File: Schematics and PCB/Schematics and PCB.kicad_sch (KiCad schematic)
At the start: 0 parts

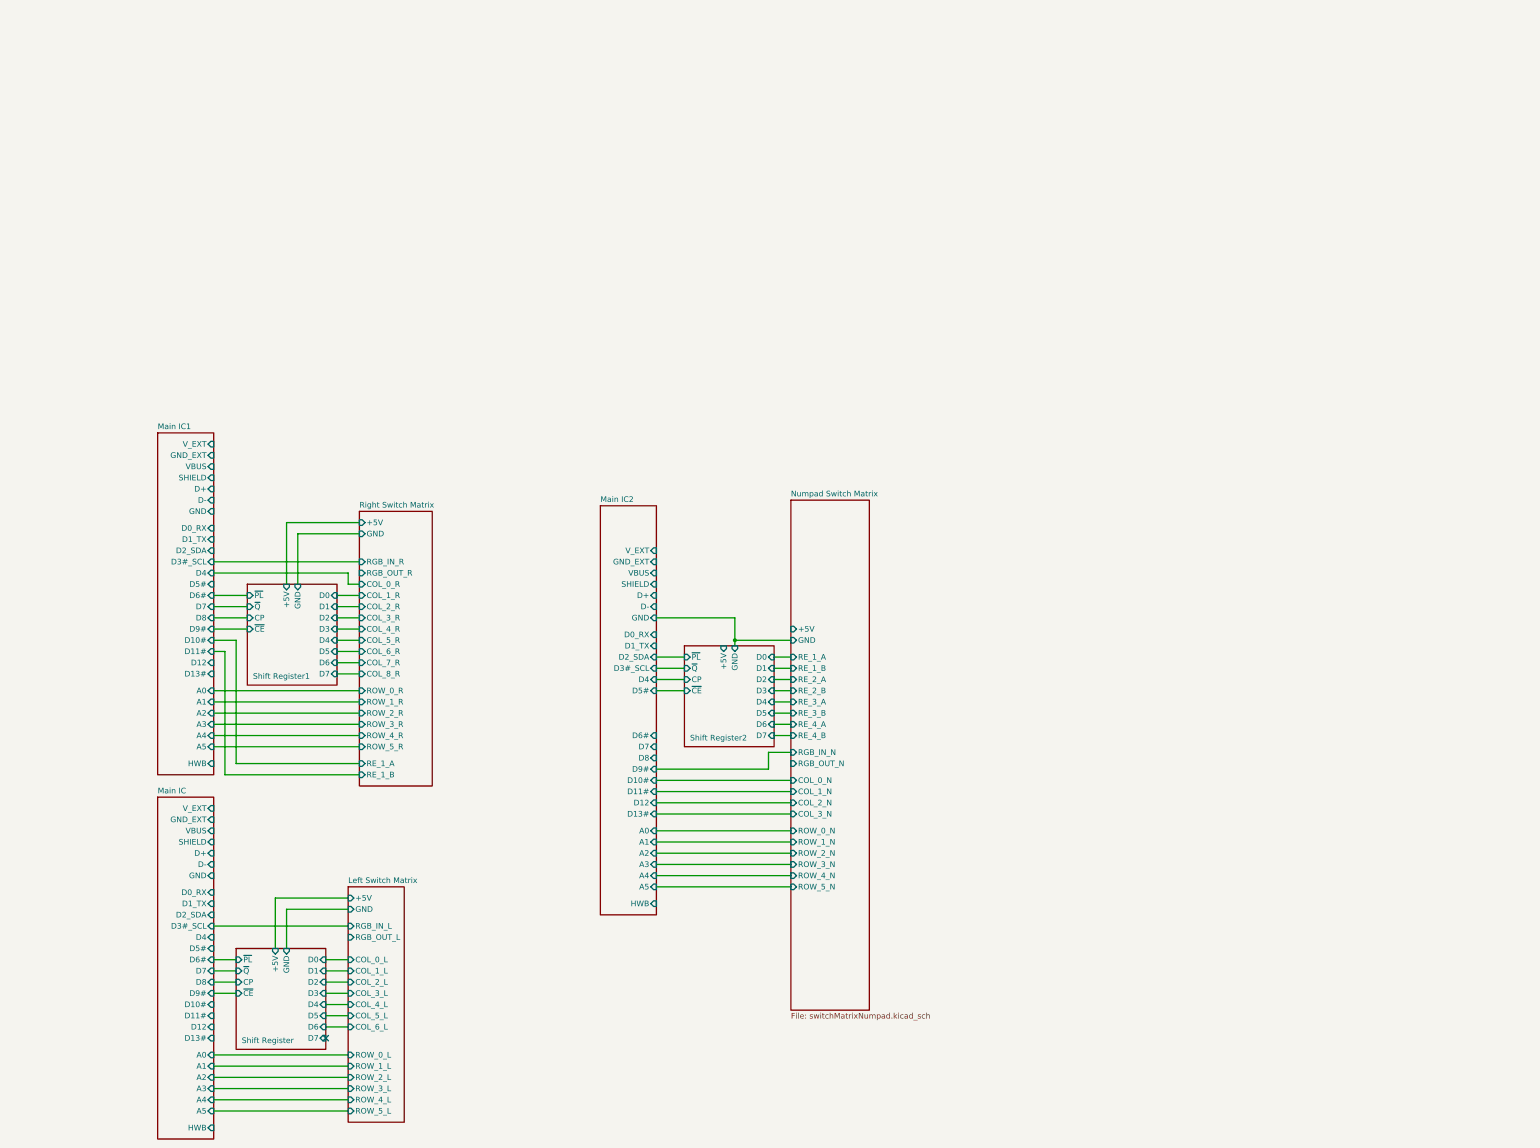
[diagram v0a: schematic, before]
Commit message: schematic progress
added li-po charge circuits and usb hub
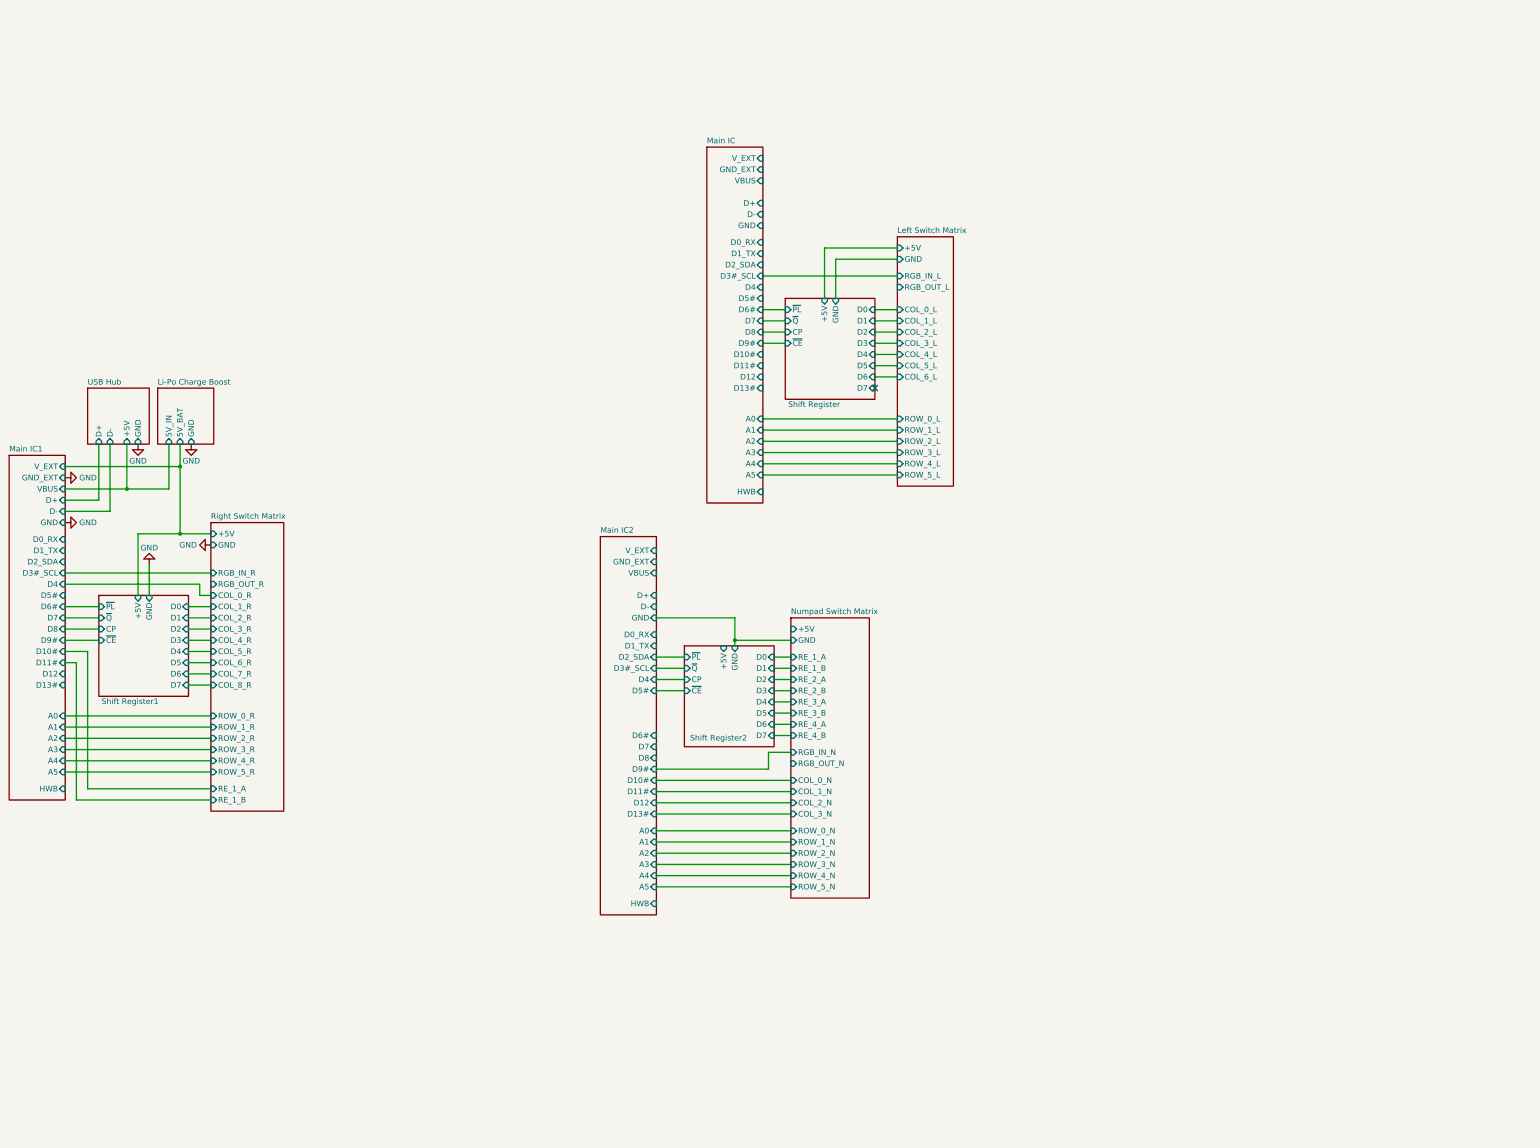
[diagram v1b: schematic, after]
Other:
- added sheet Li-Po Charge Boost (Li-Po_Charge_Boost.kicad_sch)
- added sheet USB Hub (USB_Hub.kicad_sch)
- sheet Main IC ports: added none; removed SHIELD
- sheet Main IC1 ports: added none; removed SHIELD
- sheet Main IC2 ports: added none; removed SHIELD

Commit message: compatibility commit
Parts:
- added J6: Magnetic Right, symbol Connector_Generic:Conn_01x05
- added J9: Magnetic Left, symbol Connector_Generic:Conn_01x05

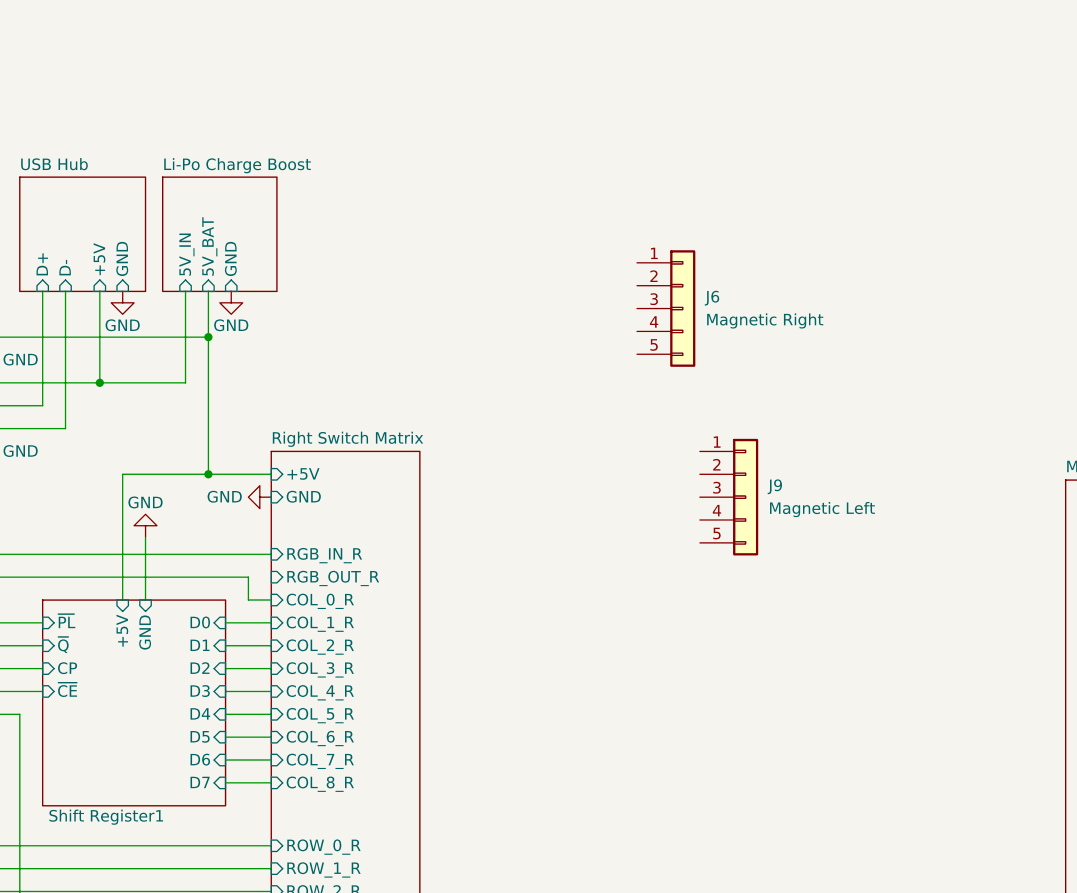
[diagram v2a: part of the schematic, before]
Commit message: Updated USB hub
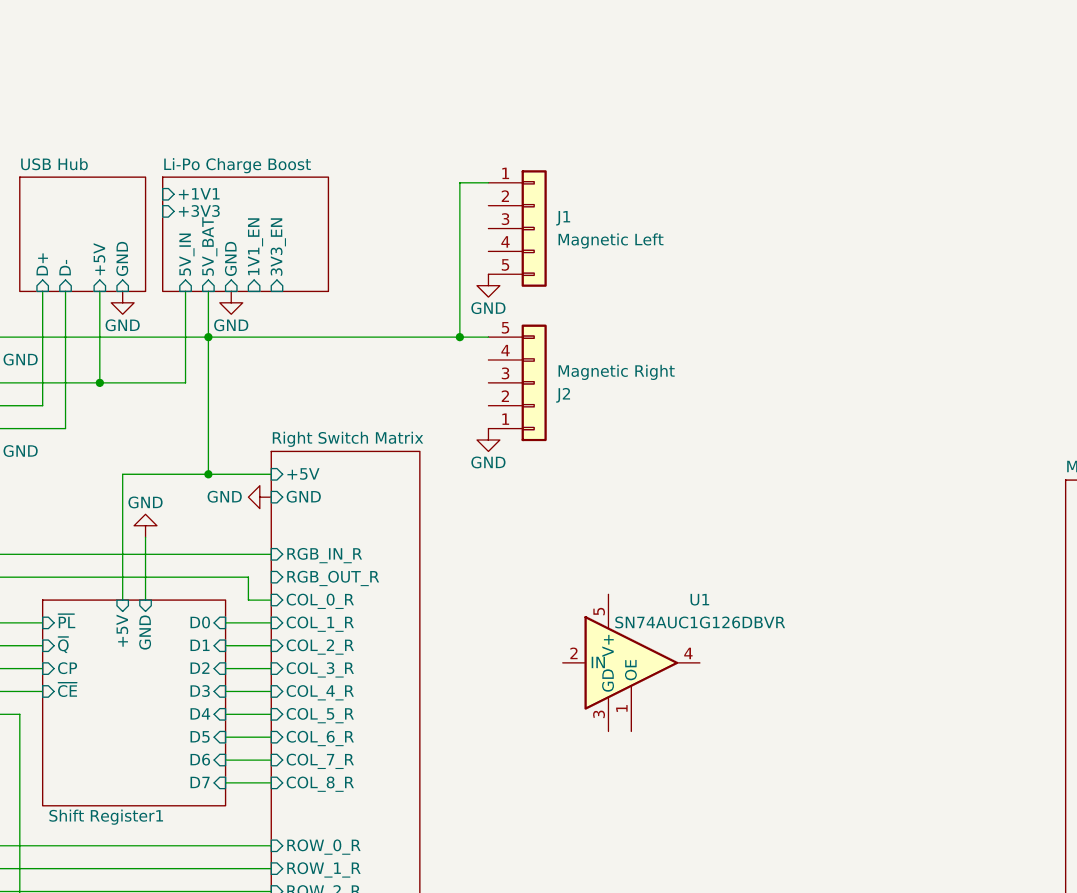
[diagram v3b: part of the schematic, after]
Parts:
- added U1: SN74AUC1G126DBVR, symbol mechpadLibrary:Tri-state_Buffer
- renumbered J9 to J1, J6 to J2
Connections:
- net GND: now also J1.5 (Pin_5), J2.1 (Pin_1)
- net Li-Po Charge Boost/5V_BAT: now also J1.1 (Pin_1), J2.5 (Pin_5)
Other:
- sheet Li-Po Charge Boost ports: added +1V1, +3V3, 1V1_EN, 3V3_EN; removed none
- moved on the sheet: J1, J2

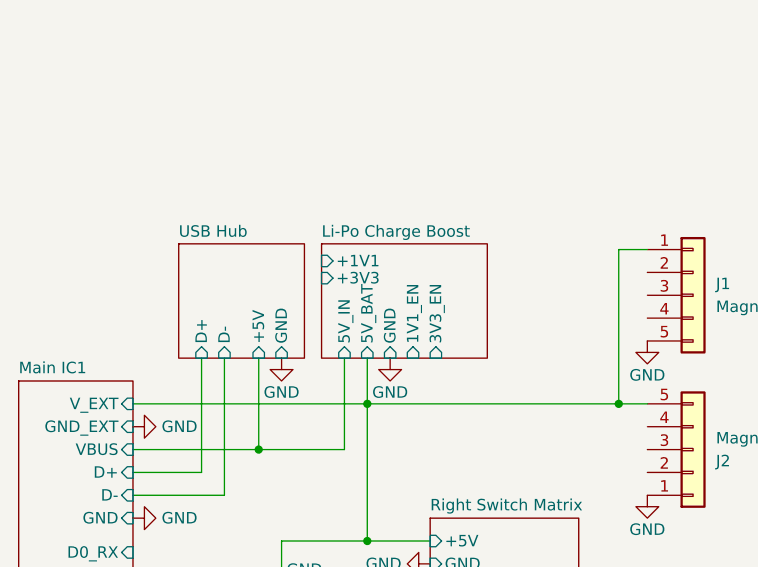
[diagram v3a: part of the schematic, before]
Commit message: bluetooth test added
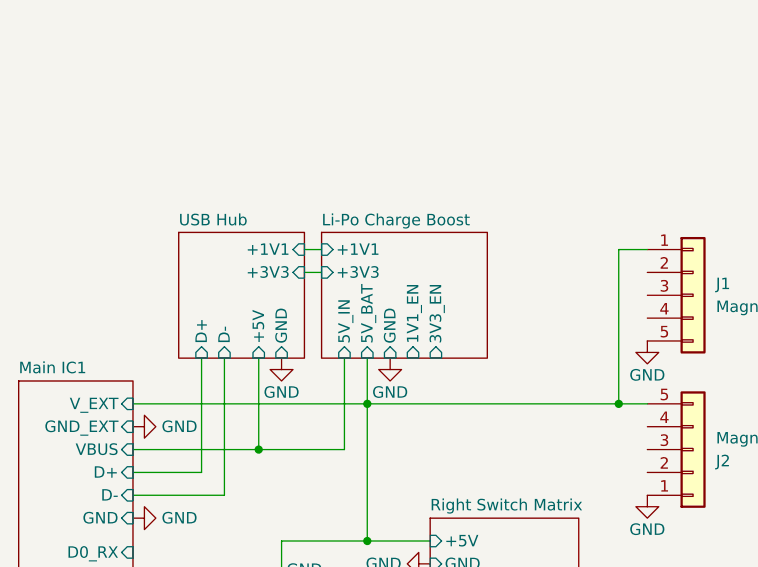
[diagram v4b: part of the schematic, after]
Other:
- sheet USB Hub ports: added +1V1, +3V3; removed none
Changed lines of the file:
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@@
+    (stroke (width 0) (type default))
+  )
+  (wire (pts (xy 47.625 17.145) (xy 49.53 17.145))
     (stroke (width 0) (type default))
   )
@@
   )
   (wire (pts (xy 56.515 81.28) (xy 61.595 81.28))
+    (stroke (width 0) (type default))
+  )
+  (wire (pts (xy 47.625 19.685) (xy 49.53 19.685))
     (stroke (width 0) (type default))
   )
@@
     )
   )
-  (sheet (at 49.53 16.51) (size 18.415 12.7)
+  (sheet (at 49.53 15.24) (size 18.415 13.97)
     (stroke (width 0.1524) (type solid))
     (fill (color 0 0 0 0.0000))
-    (property "Sheetname" "Li-Po Charge Boost" (at 49.53 15.875 0)
+    (property "Sheetname" "Li-Po Charge Boost" (at 49.53 14.605 0)
       (effects (font (size 1.27 1.27)) (justify left bottom))
     )
-    (property "Sheetfile" "Li-Po_Charge_Boost.kicad_sch" (at 68.5296 29.21 90)
+    (property "Sheetfile" "Li-Po_Charge_Boost.kicad_sch" (at 68.5296 27.94 90)
       (effects (font (size 1.27 1.27)) (justify left top) hide)
     )
@@
       (effects (font (size 1.27 1.27)) (justify left))
     )
-    (pin "+1V1" input (at 49.53 18.415 180)
-      (effects (font (size 1.27 1.27)) (justify left))
-    )
-    (pin "+3V3" input (at 49.53 20.32 180)
+    (pin "+1V1" input (at 49.53 17.145 180)
+      (effects (font (size 1.27 1.27)) (justify left))
+    )
+    (pin "+3V3" input (at 49.53 19.685 180)
       (effects (font (size 1.27 1.27)) (justify left))
     )
@@
     )
   )
-  (sheet (at 33.655 16.51) (size 13.97 12.7)
+  (sheet (at 33.655 15.24) (size 13.97 13.97)
     (stroke (width 0.1524) (type solid))
     (fill (color 0 0 0 0.0000))
-    (property "Sheetname" "USB Hub" (at 33.655 15.875 0)
+    (property "Sheetname" "USB Hub" (at 33.655 14.605 0)
       (effects (font (size 1.27 1.27)) (justify left bottom))
     )
-    (property "Sheetfile" "USB_Hub.kicad_sch" (at 49.4796 29.21 90)
+    (property "Sheetfile" "USB_Hub.kicad_sch" (at 49.4796 27.94 90)
       (effects (font (size 1.27 1.27)) (justify left top) hide)
     )
@@
       (effects (font (size 1.27 1.27)) (justify left))
     )
-    (instances
+    (pin "+3V3" input (at 47.625 19.685 0)
+      (effects (font (size 1.27 1.27)) (justify right))
+    )
+    (pin "+1V1" input (at 47.625 17.145 0)
+      (effects (font (size 1.27 1.27)) (justify right))
+    )
+    (instances

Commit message: Right layout created
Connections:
- net Li-Po Charge Boost/5V_BAT renamed V_BAT
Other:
- removed sheet Shift Register1
- sheet Li-Po Charge Boost ports: added none; removed +1V1, +3V3, 1V1_EN, 3V3_EN
- sheet Right Switch Matrix ports: added CP, DS, RE_SW, SH_CP, ST_CP, ~{CE}, ~{PL}, ~{Q7}; removed COL_0_R, COL_1_R, COL_2_R, COL_3_R, COL_4_R, COL_5_R, COL_6_R, COL_7_R, COL_8_R, ROW_0_R, ROW_1_R, ROW_2_R, ROW_3_R, ROW_4_R, ROW_5_R
- sheet USB Hub ports: added 1V1_EN, 3V3_EN; removed none
- moved on the sheet: J1, J2

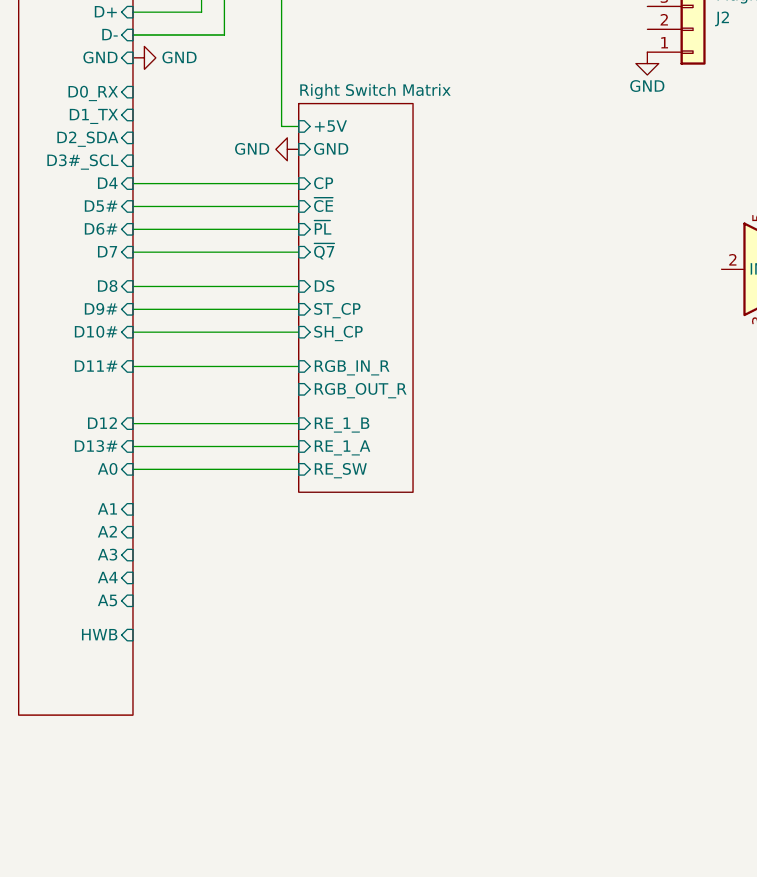
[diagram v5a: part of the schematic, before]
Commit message: Finished initial iteration of the Right layout
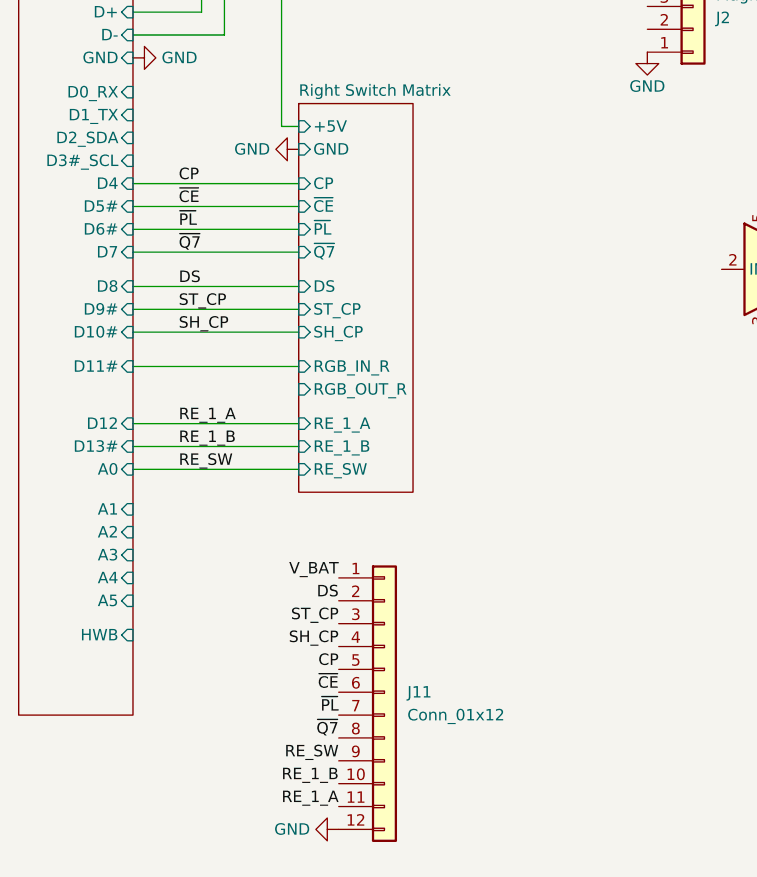
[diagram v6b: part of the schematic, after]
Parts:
- added J11: Conn_01x12, Connector_FFC-FPC:Hirose_FH12-12S-0.5SH_1x12-1MP_P0.50mm_Horizontal, symbol Connector_Generic:Conn_01x12
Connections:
- net GND: now also J11.12 (Pin_12)
- net V_BAT: now also J11.1 (Pin_1)
- new net CP: J11.5 (Pin_5)
- new net DS: J11.2 (Pin_2)
- new net RE_1_A: J11.11 (Pin_11)
- new net RE_1_B: J11.10 (Pin_10)
- new net RE_SW: J11.9 (Pin_9)
- new net SH_CP: J11.4 (Pin_4)
- new net ST_CP: J11.3 (Pin_3)
- new net ~{CE}: J11.6 (Pin_6)
- new net ~{PL}: J11.7 (Pin_7)
- new net ~{Q7}: J11.8 (Pin_8)
